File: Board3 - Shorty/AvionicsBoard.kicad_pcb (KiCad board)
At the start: 2 copper layers, 157.4 x 59 mm, 80 parts, among them J1 USB_A, J10 I2C, J11 UART, J12 RF IN, J2 Conn_01x02, J3 SWD, J4 7.2V, J5 SPI, J6 Micro_SD_Card, J7 RF IN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

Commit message: Layout
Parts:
- removed 7.2v IN: 7.2V, Pin_Headers:Pin_Header_Straight_1x02_Pitch2.54mm
- removed D2: LED, LEDs:LED_1206
- removed F1: Fuse, Capacitors_SMD:C_1206
- removed FDBK: FDBK, Pin_Headers:Pin_Header_Straight_2x03_Pitch2.54mm
- removed G***: LOGO, RocketShopLogos:RocketShopGraphicLogo
- removed G***: LOGO, RocketShopLogos:QRcode
- removed G***: LOGO, RocketShopLogos:thumbsup
- removed I2C: I2C, Pin_Headers:Pin_Header_Straight_1x03_Pitch2.54mm
- removed PWM: PWM, Pin_Headers:Pin_Header_Straight_2x02_Pitch2.54mm
- removed R4: 2.2K, Resistors_SMD:R_0805
- removed R5, R6: 100K, Resistors_SMD:R_0603_HandSoldering
- removed R9: 10K, Resistors_SMD:R_0805
- removed REF** (x4): MountingHole_2.5mm_Pad, Mounting_Holes:MountingHole_2.5mm_Pad
- removed REF***: ESD-Logo_13.2x12mm_SilkScreen, Symbols:ESD-Logo_13.2x12mm_SilkScreen
- removed SPI: SPI, Pin_Headers:Pin_Header_Straight_1x04_Pitch2.54mm
- removed SWD: SWD, Pin_Headers:Pin_Header_Straight_1x04_Pitch2.54mm
- removed U3: MCP73831, TO_SOT_Packages_SMD:SOT-23-5
- removed the U4 at (140.7, 52.3)
- BT1: footprint Battery_Holders:Keystone_1058_1x2032-CoinCell -> DannysLib:BR-1225A_HB; moved to B.Cu
- moved J4 75.4 mm to (103.6, 52.7)
- moved J9 70.7 mm to (114.7, 53.1)
- moved U4 67.6 mm to (140.8, 52.3)
- moved J7 64.8 mm to (134.5, 55.1)
- moved J8 63.0 mm to (125.2, 58.2), turned to 180 degrees
- moved C8 58.6 mm to (132.3, 60.2)
- moved R1 56.1 mm to (135.5, 62.4), turned to 90 degrees
- moved BT1 52.0 mm to (160.8, 73.2), turned to 180 degrees
- moved J12 27.0 mm to (157.2, 101.1)
- moved J11 24.2 mm to (159.8, 59.8), turned to 0 degrees
- moved J3 23.3 mm to (126.1, 99.7), turned to 270 degrees
- moved C11 20.9 mm to (156.3, 55.0), turned to 270 degrees
- moved J5 20.8 mm to (142.5, 99.6), turned to 90 degrees
- moved C13 20.6 mm to (152.8, 55.0), turned to 270 degrees
- moved J10 20.2 mm to (137.3, 99.7), turned to 270 degrees
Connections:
- U1 pad 3: Net-(F1-Pad2) -> +3V3
- U4 pad 2: /D11 -> /RXD
- U4 pad 3: /D13 -> /TXD
- U5 pad 13: GND -> Net-(U5-Pad13)
- U5 pad 14: /B+ -> Net-(U5-Pad14)
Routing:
- net +7.5V: track 60.4 -> 0.00 mm, vias 2 -> 0
- net GND: track 155.4 -> 206.5 mm, vias 30 -> 62
- net +3V3: track 42.7 -> 92.3 mm, vias 4 -> 8
- net /B+: track 0.00 -> 26.8 mm, vias 0 -> 2
- net /TXD: track 75.0 -> 96.9 mm
- net /RXD: track 77.4 -> 94.7 mm, vias 3 -> 2
- net /A3: track 17.3 -> 0.00 mm
- net /D11: track 38.3 -> 27.1 mm, vias 4 -> 1
- net Net-(J12-Pad1): track 0.00 -> 8.56 mm
- net Net-(J7-Pad1): track 0.00 -> 7.05 mm
- net Net-(R1-Pad1): track 2.58 -> 8.57 mm
- net VBUS: track 89.5 -> 83.7 mm
- net Net-(F1-Pad2): track 5.10 -> 0.00 mm
- net /SCK: track 142.0 -> 147.0 mm
- net Net-(D2-Pad1): track 3.82 -> 0.00 mm
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- added copper zone on F.Cu, net GND
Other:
- board size 157.4 x 59 mm -> 103.4 x 58.9 mm
- board text added: "12V"
- board text removed: "7.2V"
- board text removed: "RXD"
- board text removed: "TXD"

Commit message: Finishing touches on RF
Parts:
- added M2.5: MountingHole_2.7mm_M2.5_Pad, Mounting_Holes:MountingHole_2.7mm_M2.5_Pad, F.Cu at (62.2, 106.7)
- added M2.5: MountingHole_2.7mm_M2.5_Pad, Mounting_Holes:MountingHole_2.7mm_M2.5_Pad, F.Cu at (62.2, 52.7)
- added M2.5: MountingHole_2.7mm_M2.5_Pad, Mounting_Holes:MountingHole_2.7mm_M2.5_Pad, F.Cu at (162.6, 106.7)
- added M2.5: MountingHole_2.7mm_M2.5_Pad, Mounting_Holes:MountingHole_2.7mm_M2.5_Pad, F.Cu at (162.6, 52.7)
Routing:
- net +3V3: track 92.3 -> 140.4 mm
- net GND: track 206.5 -> 185.4 mm, vias 62 -> 99
- net /SDA: track 139.5 -> 120.4 mm, vias 8 -> 6
- net /SCL: track 127.1 -> 111.6 mm
- net (no net): track 18.4 -> 5.34 mm, vias 30 -> 4
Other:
- board size 103.4 x 58.9 mm -> 106.7 x 60.3 mm
- board text added: "LoRa 900MHz"

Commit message: Do some board cleanup, generate gerbs
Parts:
- added G***: LOGO, RocketShopLogos:QRcode, B.Cu at (79.8, 59.9)
- added G***: LOGO, RocketShopLogos:RocketShopGraphicLogo, B.Cu at (111.8, 81.3)
- J2: value Conn_01x02 -> XT-60
- J4: value 7.2V -> 12v
- moved D1 39.5 mm to (68.6, 53.3), turned to 270 degrees
- moved J4 31.7 mm to (72.4, 57.8)
- moved R19 10.2 mm to (95.9, 52.7), turned to 270 degrees
- moved J2 7.30 mm to (64.8, 61.0), turned to 270 degrees
- moved R20 5.90 mm to (99.1, 52.7)
- moved D4 5.70 mm to (95.9, 57.8)
- moved R21 5.70 mm to (102.2, 52.7)
- moved D5 5.66 mm to (99.1, 57.8)
- moved D6 5.54 mm to (102.2, 57.8)
- moved J9 2.72 mm to (113.0, 55.2), turned to 180 degrees
- moved J8 0.40 mm to (125.1, 57.8)
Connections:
- J2 pad 1: GND -> +12V
- J2 pad 2: VBUS -> GND
- U4 pad 16: /SDA -> Net-(U4-Pad16)
- U4 pad 17: /SCL -> Net-(U4-Pad17)
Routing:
- net VBUS: track 83.7 -> 44.4 mm, vias 3 -> 2
- net /D10: track 42.9 -> 30.3 mm
- net /D9: track 34.4 -> 24.2 mm
- net /D7: track 24.1 -> 31.6 mm, vias 2 -> 0
- net +12V: track 4.38 -> 11.6 mm
- net /D6: track 25.3 -> 32.1 mm, vias 2 -> 0
- net /D12: track 27.3 -> 32.9 mm, vias 2 -> 0
- net /A2: track 32.4 -> 34.3 mm
- net GND: track 185.4 -> 186.8 mm, vias 99 -> 60
- net Net-(D4-Pad1): track 3.39 -> 2.48 mm
- net (no net): vias 4 -> 31
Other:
- board text added: "A1"
- board text added: "A2"
- board text added: "D10"
- board text added: "D9"
- board text added: "POWER IN"
- board text added: "Power"
- board text removed: "7-20V"
- board text removed: "A2,A1"
- board text removed: "D9,10"

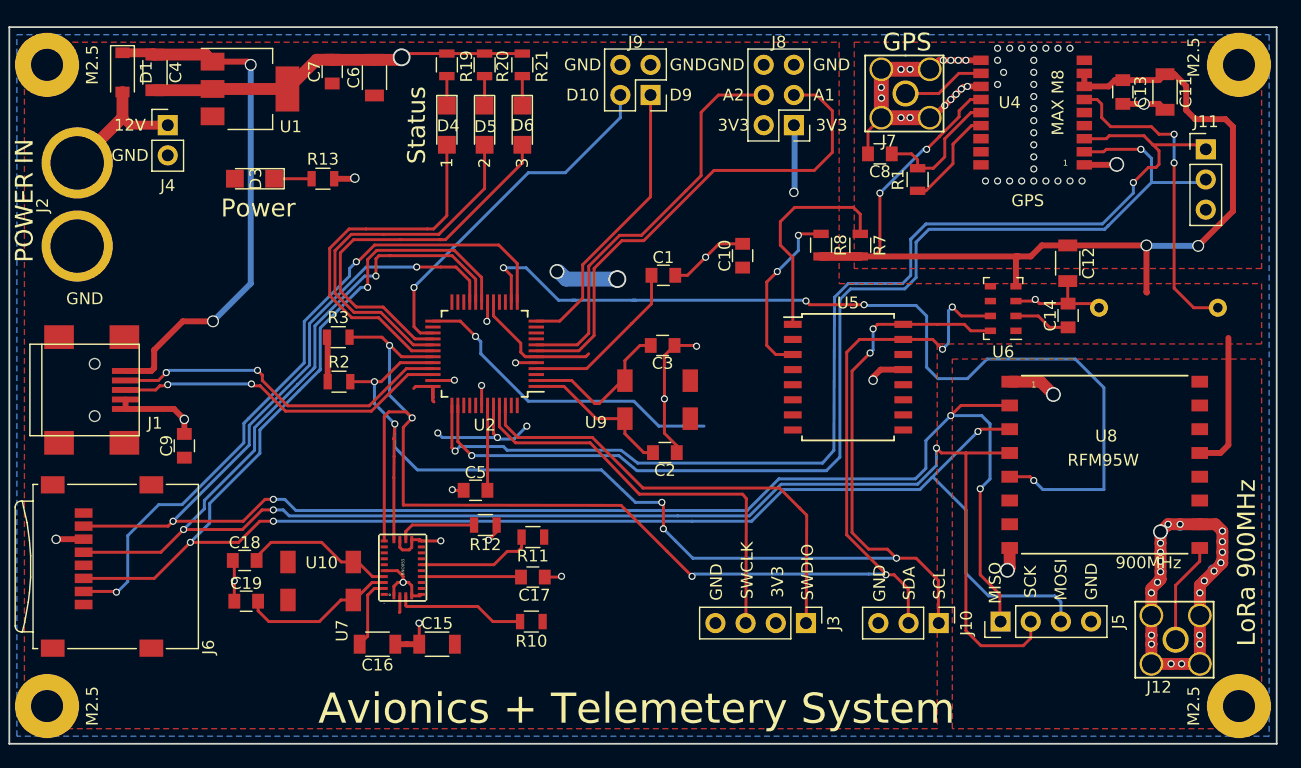
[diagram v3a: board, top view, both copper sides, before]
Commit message: Add buzzer, LorA interrupt and reset lines, fix issue with USB and battery power, reduce RF path lengths, add better microstrip matching for LoRa and GPS, create ALLPCB BOM
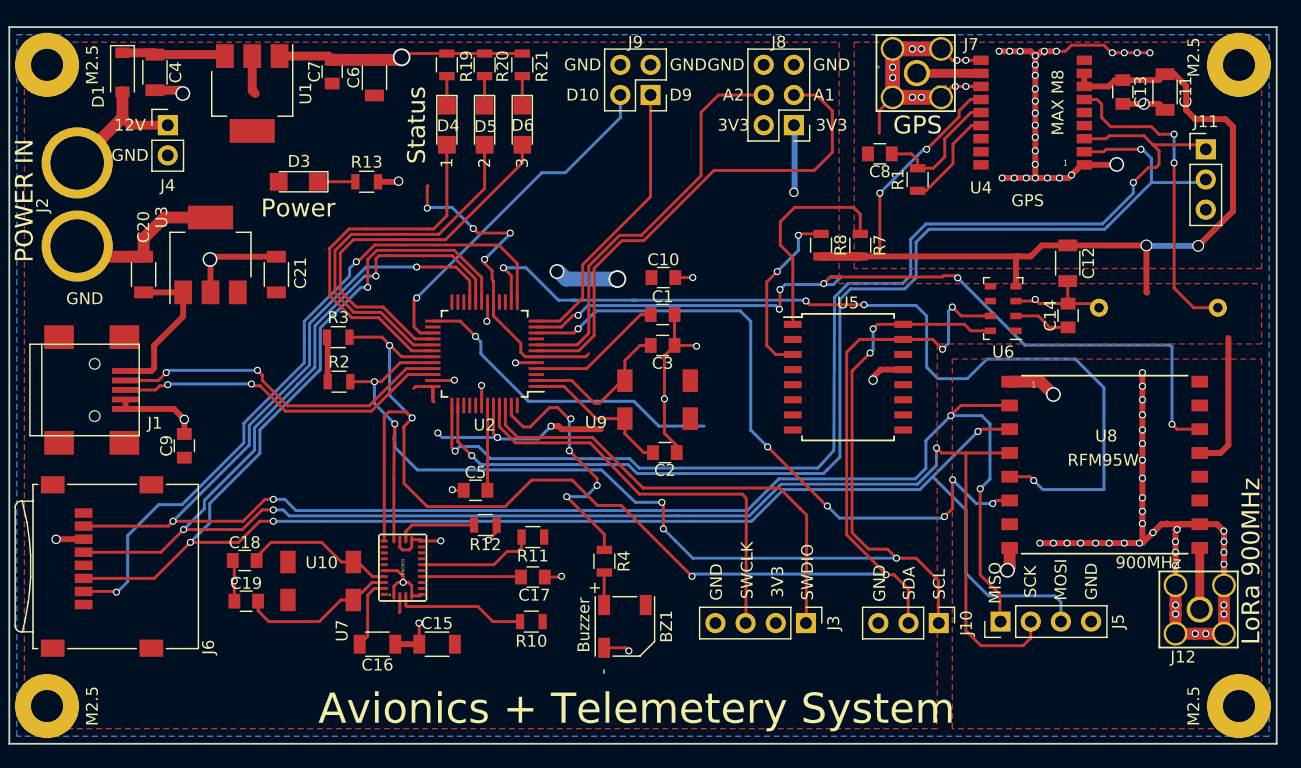
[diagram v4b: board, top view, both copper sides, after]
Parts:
- added BZ1: Buzzer, DannysLib:CUI_CMT-5023S-SMT, F.Cu at (110.9, 100.0)
- added C20: 10u, Capacitors_SMD:C_1206, F.Cu at (70.4, 70.4)
- added C21: 10u, Capacitors_SMD:C_1206, F.Cu at (81.5, 70.4)
- added R4: 330, Resistors_SMD:R_0805, F.Cu at (109.1, 94.5)
- added U3: MCP1825S, TO_SOT_Packages_SMD:SOT-223-3_TabPin2, F.Cu at (76.0, 68.7)
- U1: value TL1963 -> LT1117CST-3.3#TRPBF
- moved C10 6.92 mm to (114.1, 70.6), turned to 0 degrees
- moved D3 3.69 mm to (83.4, 62.5)
- moved R13 3.69 mm to (89.1, 62.5)
- moved C1 3.30 mm to (114.0, 73.7)
- moved J12 3.25 mm to (159.3, 98.6)
- moved J7 1.96 mm to (135.4, 53.4)
- moved U1 0.43 mm to (79.5, 55.1), turned to 270 degrees
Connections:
- C4 pad 1: VBUS -> Net-(C4-Pad1)
- D1 pad 1: VBUS -> Net-(C4-Pad1)
- U1 pad 1: VBUS -> GND
- U1 pad 2: GND -> +3V3
- U1 pad 3: +3V3 -> Net-(C4-Pad1)
- U8 pad 14: Net-(U8-Pad14) -> /D8
- U8 pad 6: Net-(U8-Pad6) -> /A4
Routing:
- net /D8: track 0.00 -> 71.3 mm, vias 0 -> 6
- net GND: track 186.8 -> 253.7 mm, vias 60 -> 96
- net /A4: track 0.00 -> 56.9 mm, vias 0 -> 6
- net VBUS: track 44.4 -> 13.2 mm, vias 2 -> 0
- net +3V3: track 140.4 -> 167.0 mm, vias 8 -> 12
- net /A5: track 0.00 -> 22.7 mm, vias 0 -> 4
- net Net-(C4-Pad1): track 0.00 -> 9.04 mm
- net Net-(J12-Pad1): track 8.56 -> 5.18 mm
- net /AREF: track 14.4 -> 11.5 mm
- net Net-(BZ1-Pad1): track 0.00 -> 2.75 mm
- net Net-(J7-Pad1): track 7.05 -> 5.43 mm
- net /SDA: track 120.4 -> 121.2 mm
- net /D10: track 30.3 -> 29.7 mm
- net (no net): track 5.34 -> 5.36 mm, vias 31 -> 2
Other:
- board text added: "Danny Mallek 2019"
- board text removed: "Danny Mallek 2018"

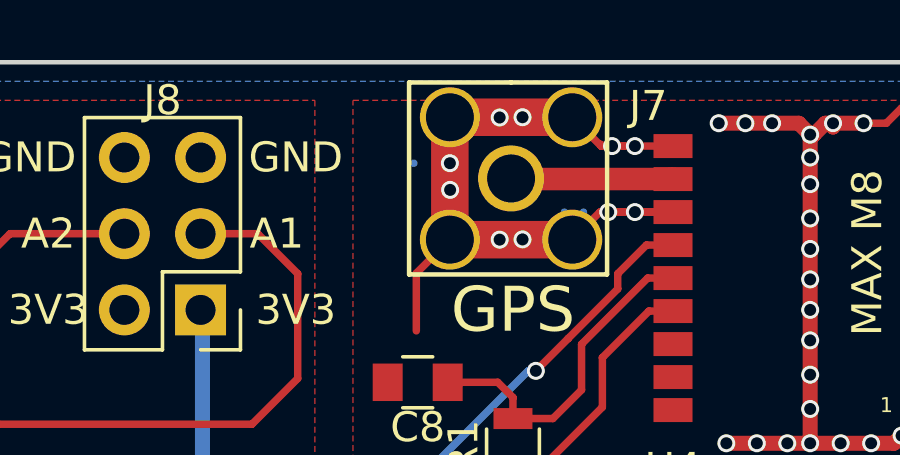
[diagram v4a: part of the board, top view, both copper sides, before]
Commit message: Update cost option 4
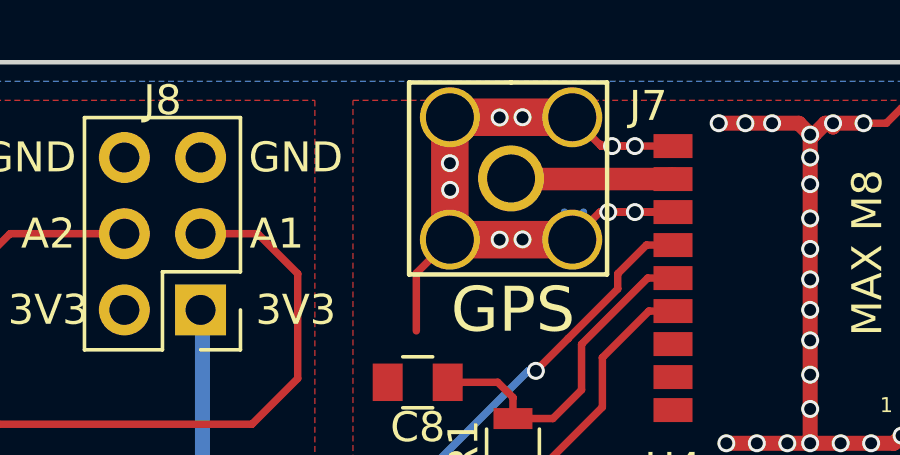
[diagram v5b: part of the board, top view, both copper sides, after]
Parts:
- added G***: LOGO, RocketShopLogos:ManifestLabs, B.Cu at (110.6, 69.1)

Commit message: Add Cyclone Rocketry Logo, generate gerbers
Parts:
- removed the G*** at (111.8, 81.3)
- removed the G*** at (110.6, 69.1)
- added G***: LOGO, RocketShopLogos:CycloneRocketryLogo, B.Cu at (115.2, 80.9)

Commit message: dsfafdsa
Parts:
- removed M2.5 (x4): MountingHole_2.7mm_M2.5_Pad, Mounting_Holes:MountingHole_2.7mm_M2.5_Pad
- added C22: 100n, Capacitors_SMD:C_0805, F.Cu at (145.9, 69.1)
- added J13: SD_CS, Pin_Headers:Pin_Header_Straight_1x01_Pitch2.54mm, F.Cu at (78.9, 103.1)
- added J14: CHASSIS LED, Pin_Headers:Pin_Header_Straight_1x01_Pitch2.54mm, F.Cu at (90.7, 58.7)
- added J15: CHASSIS GND, Mounting_Holes:MountingHole_2.5mm_Pad, F.Cu at (62.2, 106.7)
- added J16: CHASSIS GND, Mounting_Holes:MountingHole_2.5mm_Pad, F.Cu at (162.6, 106.7)
- added J17: CHASSIS GND, Mounting_Holes:MountingHole_2.5mm_Pad, F.Cu at (162.6, 52.7)
- added J18: CHASSIS GND, Mounting_Holes:MountingHole_2.5mm_Pad, F.Cu at (62.2, 52.7)
- C12: value 1u -> 10u
- C14: value .1u -> 100n
- J12, J7: footprint FoxWestern:SMA_TH -> DannysLib:SMA_TH
- moved J7 0.57 mm to (134.9, 53.4)
- moved G*** 0.39 mm to (80.1, 59.9)
- moved J12 0.26 mm to (159.3, 98.8)
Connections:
- J6 pad 9: Net-(J6-Pad9) -> GND
- U5 pad 13: Net-(U5-Pad13) -> GND
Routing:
- net /D4: track 58.2 -> 71.5 mm
- net GND: track 253.7 -> 260.5 mm, vias 96 -> 102
- net /D7: track 31.6 -> 37.0 mm
- net Net-(U5-Pad13): track 3.06 -> 0.00 mm, vias 1 -> 0
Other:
- board text added: "CHASSIS LED"
- board text added: "M2.5"
